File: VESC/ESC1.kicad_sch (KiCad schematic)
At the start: 37 parts, among them Q1 SP40N03GNJ, Q10 SP40N03GNJ, Q17 SP40N03GNJ, Q18 SP40N03GNJ, Q5 SP40N03GNJ, Q9 SP40N03GNJ, U4 AT32F421G8U7, U8 NSG2065Q

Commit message: Added fabrication files
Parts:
- R17, R29, R41: value 75K -> 10K
- R21, R30, R42: value 10K -> 1K
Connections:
- net +8V renamed +10V
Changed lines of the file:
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@@
 			)
 		)
-		(property "Value" "10K"
+		(property "Value" "1K"
 			(at 264.16 58.4199 0)
 			(show_name no)
@@
 			)
 		)
-		(property "Value" "75K"
+		(property "Value" "10K"
 			(at 264.16 36.8299 0)
 			(show_name no)
@@
 			)
 		)
-		(property "Value" "10K"
+		(property "Value" "1K"
 			(at 212.09 58.4199 0)
 			(show_name no)
@@
 	)
 	(symbol
-		(lib_id "power:+8V")
-		(at 109.22 119.38 0)
-		(unit 1)
-		(body_style 1)
-		(exclude_from_sim no)
-		(in_bom yes)
-		(on_board yes)
-		(in_pos_files yes)
-		(dnp no)
-		(fields_autoplaced yes)
-		(property "Reference" "#PWR056"
-			(at 109.22 123.19 0)
-			(hide yes)
-			(show_name no)
-			(do_not_autoplace no)
-			(effects
-				(font
-					(size 1.27 1.27)
-				)
-			)
-		)
-		(property "Value" "+8V"
-			(at 109.22 114.3 0)
-			(show_name no)
-			(do_not_autoplace no)
-			(effects
-				(font
-					(size 1.27 1.27)
-				)
-			)
-		)
-		(property "Footprint" ""
-			(at 109.22 119.38 0)
-			(hide yes)
-			(show_name no)
-			(do_not_autoplace no)
-			(effects
-				(font
-					(size 1.27 1.27)
-				)
-			)
-		)
-		(property "Datasheet" ""
-			(at 109.22 119.38 0)
-			(hide yes)
-			(show_name no)
-			(do_not_autoplace no)
-			(effects
-				(font
-					(size 1.27 1.27)
-				)
-			)
-		)
-		(property "Description" "Power symbol creates a global label with name \"+8V\""
-			(at 109.22 119.38 0)
-			(hide yes)
-			(show_name no)
-			(do_not_autoplace no)
-			(effects
-				(font
-					(size 1.27 1.27)
-				)
-			)
-		)
-		(pin "1"
-		)
-		(instances
-			(project "VENDETTAESC"
-				(path "/62497189-72eb-441b-9043-ca0a95596c6f/7c9e156b-b536-46fa-851a-311dd633243a"
-					(reference "#PWR058")
-					(unit 1)
-				)
-				(path "/62497189-72eb-441b-9043-ca0a95596c6f/c4194d8a-4081-4750-8aa5-45e80972e9ea"
-					(reference "#PWR056")
-					(unit 1)
-				)
-				(path "/62497189-72eb-441b-9043-ca0a95596c6f/c6d0038e-73b1-4107-979d-7d477f3b42f0"
-					(reference "#PWR059")
-					(unit 1)
-				)
-				(path "/62497189-72eb-441b-9043-ca0a95596c6f/f855ef8c-a86d-4f49-b472-4c306de56e33"
-					(reference "#PWR057")
-					(unit 1)
-				)
-			)
-		)
-	)
-	(symbol
 		(lib_id "Device:R")
 		(at 175.26 128.27 270)
@@
 			)
 		)
-		(property "Value" "10K"
+		(property "Value" "1K"
 			(at 238.76 58.4199 0)
 			(show_name no)
@@
 			)
 		)
-		(property "Value" "75K"
+		(property "Value" "10K"
 			(at 212.09 36.8299 0)
 			(show_name no)
@@
 	)
 	(symbol
+		(lib_id "power:+8V")
+		(at 35.56 119.38 0)
+		(unit 1)
+		(body_style 1)
+		(exclude_from_sim no)
+		(in_bom yes)
+		(on_board yes)
+		(in_pos_files yes)
+		(dnp no)
+		(property "Reference" "#PWR064"
+			(at 35.56 123.19 0)
+			(hide yes)
+			(show_name no)
+			(do_not_autoplace no)
+			(effects
+				(font
+					(size 1.27 1.27)
+				)
+			)
+		)
+		(property "Value" "+10V"
+			(at 33.02 114.554 0)
+			(show_name no)
+			(do_not_autoplace no)
+			(effects
+				(font
+					(size 1.27 1.27)
+				)
+				(justify left)
+			)
+		)
+		(property "Footprint" ""
+			(at 35.56 119.38 0)
+			(hide yes)
+			(show_name no)
+			(do_not_autoplace no)
+			(effects
+				(font
+					(size 1.27 1.27)
+				)
+			)
+		)
+		(property "Datasheet" ""
+			(at 35.56 119.38 0)
+			(hide yes)
+			(show_name no)
+			(do_not_autoplace no)
+			(effects
+				(font
+					(size 1.27 1.27)
+				)
+			)
+		)
+		(property "Description" "Power symbol creates a global label with name \"+8V\""
+			(at 35.56 119.38 0)
+			(hide yes)
+			(show_name no)
+			(do_not_autoplace no)
+			(effects
+				(font
+					(size 1.27 1.27)
+				)
+			)
+		)
+		(pin "1"
+		)
+		(instances
+			(project "VENDETTAESC"
+				(path "/62497189-72eb-441b-9043-ca0a95596c6f/7c9e156b-b536-46fa-851a-311dd633243a"
+					(reference "#PWR066")
+					(unit 1)
+				)
+				(path "/62497189-72eb-441b-9043-ca0a95596c6f/c4194d8a-4081-4750-8aa5-45e80972e9ea"
+					(reference "#PWR064")
+					(unit 1)
+				)
+				(path "/62497189-72eb-441b-9043-ca0a95596c6f/c6d0038e-73b1-4107-979d-7d477f3b42f0"
+					(reference "#PWR067")
+					(unit 1)
+				)
+				(path "/62497189-72eb-441b-9043-ca0a95596c6f/f855ef8c-a86d-4f49-b472-4c306de56e33"
+					(reference "#PWR065")
+					(unit 1)
+				)
+			)
+		)
+	)
+	(symbol
 		(lib_id "Device:C")
 		(at 128.27 142.24 270)
@@
 	)
 	(symbol
+		(lib_id "power:+8V")
+		(at 109.22 119.38 0)
+		(unit 1)
+		(body_style 1)
+		(exclude_from_sim no)
+		(in_bom yes)
+		(on_board yes)
+		(in_pos_files yes)
+		(dnp no)
+		(property "Reference" "#PWR056"
+			(at 109.22 123.19 0)
+			(hide yes)
+			(show_name no)
+			(do_not_autoplace no)
+			(effects
+				(font
+					(size 1.27 1.27)
+				)
+			)
+		)
+		(property "Value" "+10V"
+			(at 106.68 114.554 0)
+			(show_name no)
+			(do_not_autoplace no)
+			(effects
+				(font
+					(size 1.27 1.27)
+				)
+				(justify left)
+			)
+		)
+		(property "Footprint" ""
+			(at 109.22 119.38 0)
+			(hide yes)
+			(show_name no)
+			(do_not_autoplace no)
+			(effects
+				(font
+					(size 1.27 1.27)
+				)
+			)
+		)
+		(property "Datasheet" ""
+			(at 109.22 119.38 0)
+			(hide yes)
+			(show_name no)
+			(do_not_autoplace no)
+			(effects
+				(font
+					(size 1.27 1.27)
+				)
+			)
+		)
+		(property "Description" "Power symbol creates a global label with name \"+8V\""
+			(at 109.22 119.38 0)
+			(hide yes)
+			(show_name no)
+			(do_not_autoplace no)
+			(effects
+				(font
+					(size 1.27 1.27)
+				)
+			)
+		)
+		(pin "1"
+		)
+		(instances
+			(project "VENDETTAESC"
+				(path "/62497189-72eb-441b-9043-ca0a95596c6f/7c9e156b-b536-46fa-851a-311dd633243a"
+					(reference "#PWR058")
+					(unit 1)
+				)
+				(path "/62497189-72eb-441b-9043-ca0a95596c6f/c4194d8a-4081-4750-8aa5-45e80972e9ea"
+					(reference "#PWR056")
+					(unit 1)
+				)
+				(path "/62497189-72eb-441b-9043-ca0a95596c6f/c6d0038e-73b1-4107-979d-7d477f3b42f0"
+					(reference "#PWR059")
+					(unit 1)
+				)
+				(path "/62497189-72eb-441b-9043-ca0a95596c6f/f855ef8c-a86d-4f49-b472-4c306de56e33"
+					(reference "#PWR057")
+					(unit 1)
+				)
+			)
+		)
+	)
+	(symbol
 		(lib_id "Connector:TestPoint")
 		(at 166.37 54.61 270)
@@
 			)
 		)
-		(property "Value" "75K"
+		(property "Value" "10K"
 			(at 238.76 36.8299 0)
 			(show_name no)
@@
 					(unit 1)
 				)
-			)
-		)
-	)
-	(symbol
-		(lib_id "power:+8V")
-		(at 35.56 119.38 0)
-		(unit 1)
-		(body_style 1)
-		(exclude_from_sim no)
-		(in_bom yes)
-		(on_board yes)
-		(in_pos_files yes)
-		(dnp no)
-		(fields_autoplaced yes)
-		(property "Reference" "#PWR064"
-			(at 35.56 123.19 0)
-			(hide yes)
-			(show_name no)
-			(do_not_autoplace no)
-			(effects
-				(font
-					(size 1.27 1.27)
-				)
-			)
-		)
-		(property "Value" "+8V"
-			(at 35.56 114.3 0)
-			(show_name no)
-			(do_not_autoplace no)
-			(effects
-				(font
-					(size 1.27 1.27)
-				)
-			)
-		)
-		(property "Footprint" ""
-			(at 35.56 119.38 0)
-			(hide yes)
-			(show_name no)
-			(do_not_autoplace no)
-			(effects
-				(font
-					(size 1.27 1.27)
-				)
-			)
-		)
-		(property "Datasheet" ""
-			(at 35.56 119.38 0)
-			(hide yes)
-			(show_name no)
-			(do_not_autoplace no)
-			(effects
-				(font
-					(size 1.27 1.27)
-				)
-			)
-		)
-		(property "Description" "Power symbol creates a global label with name \"+8V\""
-			(at 35.56 119.38 0)
-			(hide yes)
-			(show_name no)
-			(do_not_autoplace no)
-			(effects
-				(font
-					(size 1.27 1.27)
-				)
-			)
-		)
-		(pin "1"
-		)
-		(instances
-			(project "VENDETTAESC"
-				(path "/62497189-72eb-441b-9043-ca0a95596c6f/7c9e156b-b536-46fa-851a-311dd633243a"
-					(reference "#PWR066")
-					(unit 1)
-				)
-				(path "/62497189-72eb-441b-9043-ca0a95596c6f/c4194d8a-4081-4750-8aa5-45e80972e9ea"
-					(reference "#PWR064")
-					(unit 1)
-				)
-				(path "/62497189-72eb-441b-9043-ca0a95596c6f/c6d0038e-73b1-4107-979d-7d477f3b42f0"
-					(reference "#PWR067")
-					(unit 1)
-				)
-				(path "/62497189-72eb-441b-9043-ca0a95596c6f/f855ef8c-a86d-4f49-b472-4c306de56e33"
-					(reference "#PWR065")
-					(unit 1)
-				)

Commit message: Added telemetery feature for ESC
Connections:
- net TEL: now reaches U4.8 (PA2)
- no-connect marks 14 -> 13
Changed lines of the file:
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@@
-	)
-	(no_connect
-		(at 85.09 50.8)
 	)
 	(no_connect
@@
 		)
 	)
+	(global_label "TEL"
+		(shape input)
+		(at 85.09 50.8 180)
+		(fields_autoplaced yes)
+		(effects
+			(font
+				(size 1.27 1.27)
+			)
+			(justify right)
+		)
+		(property "Intersheetrefs" "${INTERSHEET_REFS}"
+			(at 78.9601 50.8 0)
+			(hide yes)
+			(show_name no)
+			(do_not_autoplace no)
+			(effects
+				(font
+					(size 1.27 1.27)
+				)
+				(justify right)
+			)
+		)
+	)

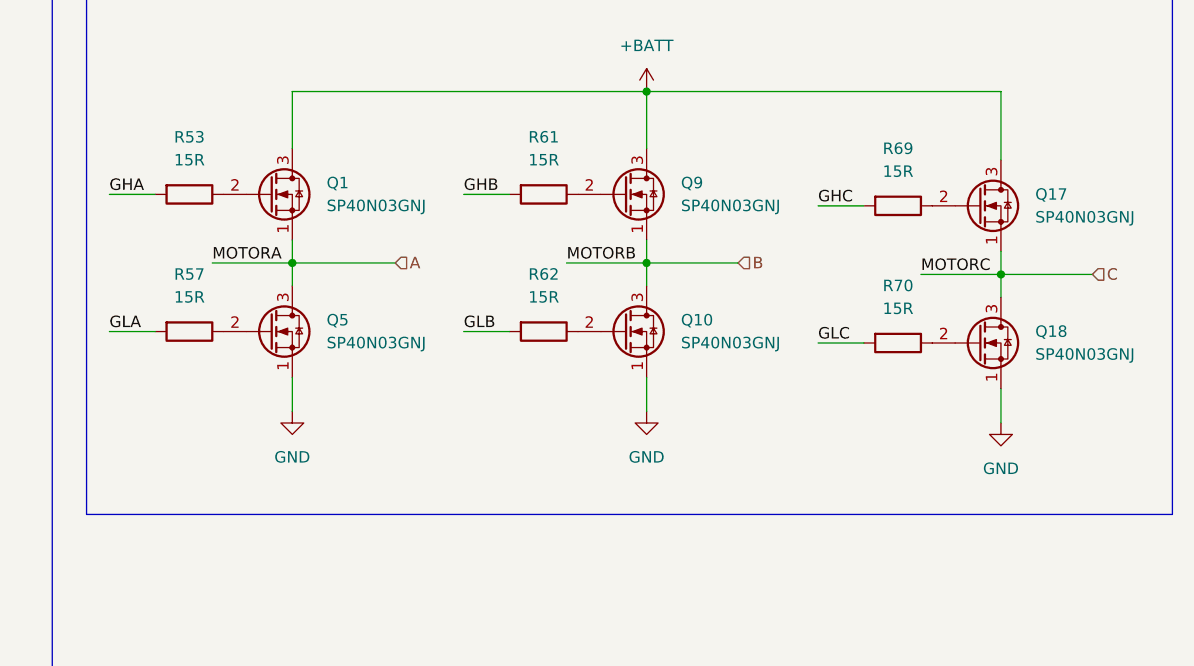
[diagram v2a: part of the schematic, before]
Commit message: Added telemetery feature for ESC
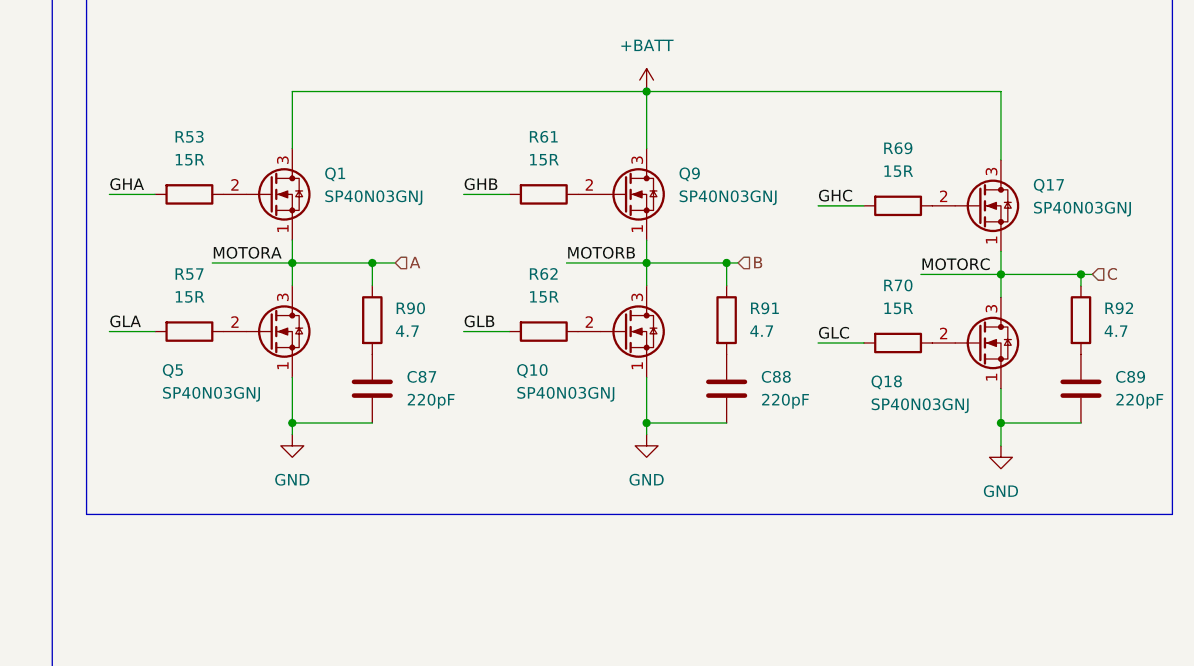
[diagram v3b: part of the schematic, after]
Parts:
- added C87, C88, C89: 220pF, Capacitor_SMD:C_0201_0603Metric, symbol Device:C
- added R90, R91, R92: 4.7, Resistor_SMD:R_0201_0603Metric, symbol Device:R
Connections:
- net A: now also R90.1
- net B: now also R91.1
- net C: now also R92.1
- net GND: now also C87.2, C88.2, C89.2
- new net: C88.1, R91.2
- new net: C89.1, R92.2
- new net: C87.1, R90.2

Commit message: VESC Revision 2.0
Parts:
- added C75: 100nF, Capacitor_SMD:C_0402_1005Metric, symbol Device:C
- C11, C15, C19, C71, C87, C88, C89: footprint Capacitor_SMD:C_0201_0603Metric -> Capacitor_SMD:C_0402_1005Metric
- C67: value 470uF -> 4.7uF; footprint Capacitor_SMD:C_0201_0603Metric -> Capacitor_SMD:C_0603_1608Metric
- FB1: footprint Inductor_SMD:L_0201_0603Metric -> Inductor_SMD:L_0402_1005Metric
- R13, R17, R21, R25, R29, R30, R31, R41, R42, R43, R5, R53, R57, R61, R62, R69, R70, R9, R90, R91, R92: footprint Resistor_SMD:R_0201_0603Metric -> Resistor_SMD:R_0402_1005Metric
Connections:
- net +10V: now also C75.1
- net GND: now also C75.2
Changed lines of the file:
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@@
 	)
 	(junction
+		(at 35.56 133.35)
+		(diameter 0)
+		(color 0 0 0 0)
+	)
+	(junction
 		(at 261.62 46.99)
 		(diameter 0)
@@
 	)
 	(junction
+		(at 35.56 120.65)
+		(diameter 0)
+		(color 0 0 0 0)
+	)
+	(junction
 		(at 40.64 49.53)
 		(diameter 0)
@@
 	(wire
 		(pts
+			(xy 35.56 120.65) (xy 35.56 123.19)
+		)
+		(stroke
+			(width 0)
+			(type default)
+		)
+	)
+	(wire
+		(pts
 			(xy 205.74 143.51) (xy 210.82 143.51)
 		)
@@
 	(wire
 		(pts
+			(xy 48.26 123.19) (xy 48.26 120.65)
+		)
+		(stroke
+			(width 0)
+			(type default)
+		)
+	)
+	(wire
+		(pts
 			(xy 29.21 67.31) (xy 36.83 67.31)
 		)
@@
 	(wire
 		(pts
+			(xy 48.26 133.35) (xy 35.56 133.35)
+		)
+		(stroke
+			(width 0)
+			(type default)
+		)
+	)
+	(wire
+		(pts
 			(xy 209.55 31.75) (xy 209.55 27.94)
 		)
@@
 	(wire
 		(pts
+			(xy 48.26 120.65) (xy 35.56 120.65)
+		)
+		(stroke
+			(width 0)
+			(type default)
+		)
+	)
+	(wire
+		(pts
 			(xy 234.95 135.89) (xy 236.22 135.89)
 		)
@@
 	(wire
 		(pts
+			(xy 48.26 130.81) (xy 48.26 133.35)
+		)
+		(stroke
+			(width 0)
+			(type default)
+		)
+	)
+	(wire
+		(pts
 			(xy 236.22 60.96) (xy 236.22 66.04)
 		)
@@
 	(wire
 		(pts
+			(xy 35.56 133.35) (xy 35.56 134.62)
+		)
+		(stroke
+			(width 0)
+			(type default)
+		)
+	)
+	(wire
+		(pts
 			(xy 73.66 144.78) (xy 80.01 144.78)
 		)
@@
 	(wire
 		(pts
-			(xy 35.56 130.81) (xy 35.56 134.62)
+			(xy 35.56 130.81) (xy 35.56 133.35)
 		)
 		(stroke
@@
 	(wire
 		(pts
-			(xy 35.56 119.38) (xy 35.56 123.19)
+			(xy 35.56 119.38) (xy 35.56 120.65)
 		)
 		(stroke
@@
 			)
 		)
-		(property "Footprint" "Capacitor_SMD:C_0201_0603Metric"
+		(property "Footprint" "Capacitor_SMD:C_0402_1005Metric"
 			(at 41.6052 49.53 0)
 			(hide yes)
@@
 			)
 		)
-		(property "Footprint" "Resistor_SMD:R_0201_0603Metric"
+		(property "Footprint" "Resistor_SMD:R_0402_1005Metric"
 			(at 259.842 57.15 90)
 			(hide yes)
@@
 			)
 		)
-		(property "Footprint" "Resistor_SMD:R_0201_0603Metric"
+		(property "Footprint" "Resistor_SMD:R_0402_1005Metric"
 			(at 60.96 38.862 90)
 			(hide yes)
@@
 			)
 		)
-		(property "Footprint" "Resistor_SMD:R_0201_0603Metric"
+		(property "Footprint" "Resistor_SMD:R_0402_1005Metric"
 			(at 214.63 141.732 90)
 			(hide yes)
@@
 			)
 		)
-		(property "Footprint" "Resistor_SMD:R_0201_0603Metric"
+		(property "Footprint" "Resistor_SMD:R_0402_1005Metric"
 			(at 233.172 142.24 90)
 			(hide yes)
@@
 			)
 		)
-		(property "Footprint" "Capacitor_SMD:C_0201_0603Metric"
+		(property "Footprint" "Capacitor_SMD:C_0402_1005Metric"
 			(at 275.2852 153.67 0)
 			(hide yes)
@@
 			)
 		)
-		(property "Footprint" "Resistor_SMD:R_0201_0603Metric"
+		(property "Footprint" "Resistor_SMD:R_0402_1005Metric"
 			(at 259.842 35.56 90)
 			(hide yes)
@@
 			)
 		)
-		(property "Footprint" "Resistor_SMD:R_0201_0603Metric"
+		(property "Footprint" "Resistor_SMD:R_0402_1005Metric"
 			(at 218.44 48.768 90)
 			(hide yes)
@@
 			)
 		)
-		(property "Footprint" "Resistor_SMD:R_0201_0603Metric"
+		(property "Footprint" "Resistor_SMD:R_0402_1005Metric"
 			(at 207.772 57.15 90)
 			(hide yes)
@@
 			)
 		)
-		(property "Footprint" "Capacitor_SMD:C_0201_0603Metric"
+		(property "Footprint" "Capacitor_SMD:C_0402_1005Metric"
 			(at 68.2752 48.26 0)
 			(hide yes)
@@
 			)
 		)
-		(property "Footprint" "Resistor_SMD:R_0201_0603Metric"
+		(property "Footprint" "Resistor_SMD:R_0402_1005Metric"
 			(at 165.1 41.402 90)
 			(hide yes)
@@
 			)
 		)
-		(property "Footprint" "Capacitor_SMD:C_0201_0603Metric"
+		(property "Footprint" "Capacitor_SMD:C_0402_1005Metric"
 			(at 37.7952 74.93 0)
 			(hide yes)
@@
 			)
 		)
-		(property "Footprint" "Capacitor_SMD:C_0201_0603Metric"
+		(property "Footprint" "Capacitor_SMD:C_0402_1005Metric"
 			(at 27.6352 49.53 0)
 			(hide yes)
@@
 			)
 		)
-		(property "Footprint" "Resistor_SMD:R_0201_0603Metric"
+		(property "Footprint" "Resistor_SMD:R_0402_1005Metric"
 			(at 175.26 126.492 90)
 			(hide yes)
@@
 			)
 		)
-		(property "Footprint" "Resistor_SMD:R_0201_0603Metric"
+		(property "Footprint" "Resistor_SMD:R_0402_1005Metric"
 			(at 254 143.002 90)
 			(hide yes)
@@
 			)
 		)
-		(property "Value" "470uF"
+		(property "Value" "4.7uF"
 			(at 39.37 128.2699 0)
 			(show_name no)
@@
 			)
 		)
-		(property "Footprint" "Capacitor_SMD:C_0201_0603Metric"
+		(property "Footprint" "Capacitor_SMD:C_0603_1608Metric"
 			(at 36.5252 130.81 0)
 			(hide yes)
@@
 			)
 		)
-		(property "Footprint" "Resistor_SMD:R_0201_0603Metric"
+		(property "Footprint" "Resistor_SMD:R_0402_1005Metric"
 			(at 234.442 57.15 90)
 			(hide yes)
@@
 			)
 		)
-		(property "Footprint" "Resistor_SMD:R_0201_0603Metric"
+		(property "Footprint" "Resistor_SMD:R_0402_1005Metric"
 			(at 254 127.762 90)
 			(hide yes)
@@
 	)
 	(symbol
+		(lib_id "Device:C")
+		(at 48.26 127 0)
+		(unit 1)
+		(body_style 1)
+		(exclude_from_sim no)
+		(in_bom yes)
+		(on_board yes)
+		(in_pos_files yes)
+		(dnp no)
+		(fields_autoplaced yes)
+		(property "Reference" "C75"
+			(at 52.07 125.7299 0)
+			(show_name no)
+			(do_not_autoplace no)
+			(effects
+				(font
+					(size 1.27 1.27)
+				)
+				(justify left)
+			)
+		)
+		(property "Value" "100nF"
+			(at 52.07 128.2699 0)
+			(show_name no)
+			(do_not_autoplace no)
+			(effects
+				(font
+					(size 1.27 1.27)
+				)
+				(justify left)
+			)
+		)
+		(property "Footprint" "Capacitor_SMD:C_0402_1005Metric"
+			(at 49.2252 130.81 0)
+			(hide yes)
+			(show_name no)
+			(do_not_autoplace no)
+			(effects
+				(font
+					(size 1.27 1.27)
+				)
+			)
+		)
+		(property "Datasheet" ""
+			(at 48.26 127 0)
+			(hide yes)
+			(show_name no)
+			(do_not_autoplace no)
+			(effects
+				(font
+					(size 1.27 1.27)
+				)
+			)
+		)
+		(property "Description" "Unpolarized capacitor"
+			(at 48.26 127 0)
+			(hide yes)
+			(show_name no)
+			(do_not_autoplace no)
+			(effects
+				(font
+					(size 1.27 1.27)
+				)
+			)
+		)
+		(pin "1"
+		)
+		(pin "2"
+		)
+		(instances
+			(project "VENDETTAESC"
+				(path "/62497189-72eb-441b-9043-ca0a95596c6f/7c9e156b-b536-46fa-851a-311dd633243a"
+					(reference "C77")
+					(unit 1)
+				)
+				(path "/62497189-72eb-441b-9043-ca0a95596c6f/c4194d8a-4081-4750-8aa5-45e80972e9ea"
+					(reference "C75")
+					(unit 1)
+				)
+				(path "/62497189-72eb-441b-9043-ca0a95596c6f/c6d0038e-73b1-4107-979d-7d477f3b42f0"
+					(reference "C78")
+					(unit 1)
+				)
+				(path "/62497189-72eb-441b-9043-ca0a95596c6f/f855ef8c-a86d-4f49-b472-4c306de56e33"
+					(reference "C76")
+					(unit 1)
+				)
+			)
+		)
+	)
+	(symbol
 		(lib_name "2N7002K_5")
 		(lib_id "Transistor_FET:2N7002K")
@@
 			)
 		)
-		(property "Footprint" "Resistor_SMD:R_0201_0603Metric"
+		(property "Footprint" "Resistor_SMD:R_0402_1005Metric"
 			(at 193.802 142.24 90)
 			(hide yes)
@@
 			)
 		)
-		(property "Footprint" "Resistor_SMD:R_0201_0603Metric"
+		(property "Footprint" "Resistor_SMD:R_0402_1005Metric"
 			(at 272.542 142.24 90)
 			(hide yes)
@@
 			)
 		)
-		(property "Footprint" "Resistor_SMD:R_0201_0603Metric"
+		(property "Footprint" "Resistor_SMD:R_0402_1005Metric"
 			(at 175.26 141.732 90)
 			(hide yes)
@@
 			)
 		)
-		(property "Footprint" "Capacitor_SMD:C_0201_0603Metric"
+		(property "Footprint" "Capacitor_SMD:C_0402_1005Metric"
 			(at 196.5452 153.67 0)
 			(hide yes)
@@
 			)
 		)
-		(property "Footprint" "Resistor_SMD:R_0201_0603Metric"
+		(property "Footprint" "Resistor_SMD:R_0402_1005Metric"
 			(at 207.772 35.56 90)
 			(hide yes)
@@
 			)
 		)
-		(property "Footprint" "Resistor_SMD:R_0201_0603Metric"
+		(property "Footprint" "Resistor_SMD:R_0402_1005Metric"
 			(at 214.63 126.492 90)
 			(hide yes)
@@
 			)
 		)
-		(property "Footprint" "Resistor_SMD:R_0201_0603Metric"
+		(property "Footprint" "Resistor_SMD:R_0402_1005Metric"
 			(at 81.28 31.242 90)
 			(hide yes)
@@
 			)
 		)
-		(property "Footprint" "Resistor_SMD:R_0201_0603Metric"
+		(property "Footprint" "Resistor_SMD:R_0402_1005Metric"
 			(at 245.11 48.768 90)
 			(hide yes)
@@
 			)
 		)
-		(property "Footprint" "Inductor_SMD:L_0201_0603Metric"
+		(property "Footprint" "Inductor_SMD:L_0402_1005Metric"
 			(at 50.8 69.088 90)
 			(hide yes)
@@
 			)
 		)
-		(property "Footprint" "Resistor_SMD:R_0201_0603Metric"
+		(property "Footprint" "Resistor_SMD:R_0402_1005Metric"
 			(at 234.442 35.56 90)
 			(hide yes)
@@
 			)
 		)
-		(property "Footprint" "Capacitor_SMD:C_0201_0603Metric"
+		(property "Footprint" "Capacitor_SMD:C_0402_1005Metric"
 			(at 235.9152 153.67 0)
 			(hide yes)
@@
 			)
 		)
-		(property "Footprint" "Resistor_SMD:R_0201_0603Metric"
+		(property "Footprint" "Resistor_SMD:R_0402_1005Metric"
 			(at 270.51 48.768 90)
 			(hide yes)
